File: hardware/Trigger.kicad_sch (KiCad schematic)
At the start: 4 parts, among them U6 MCP47FEB02A0T-E/ST, U7 Opamp_Dual

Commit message: added footprints
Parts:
- C28, C30: footprint (none) -> Capacitor_SMD:C_0402_1005Metric
- U6: footprint TSSOP8_ST_MCH -> MCP47FE:TSSOP8_ST_MCH
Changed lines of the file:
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@@
 			)
 		)
-		(property "Footprint" ""
+		(property "Footprint" "Capacitor_SMD:C_0402_1005Metric"
 			(at 43.4848 96.52 0)
 			(effects
@@
 			)
 		)
-		(property "Footprint" "TSSOP8_ST_MCH"
+		(property "Footprint" "MCP47FE:TSSOP8_ST_MCH"
 			(at 60.96 83.82 0)
 			(effects
@@
 			)
 		)
-		(property "Footprint" ""
+		(property "Footprint" "Capacitor_SMD:C_0402_1005Metric"
 			(at 141.9352 72.39 0)
 			(effects

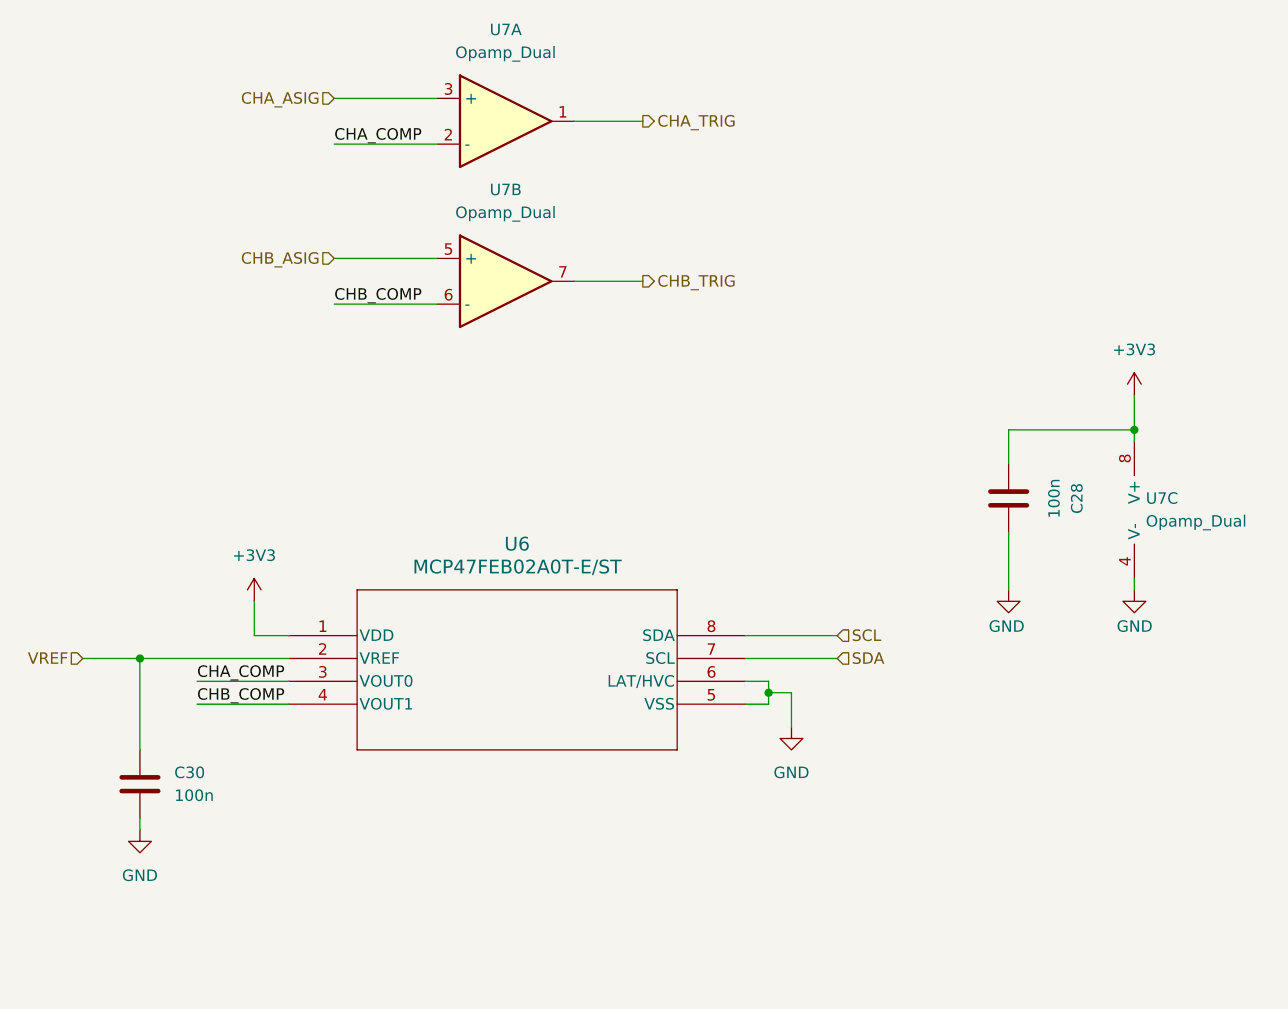
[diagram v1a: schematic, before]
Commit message: feat(hardware): Add test point connections + update PCB layout
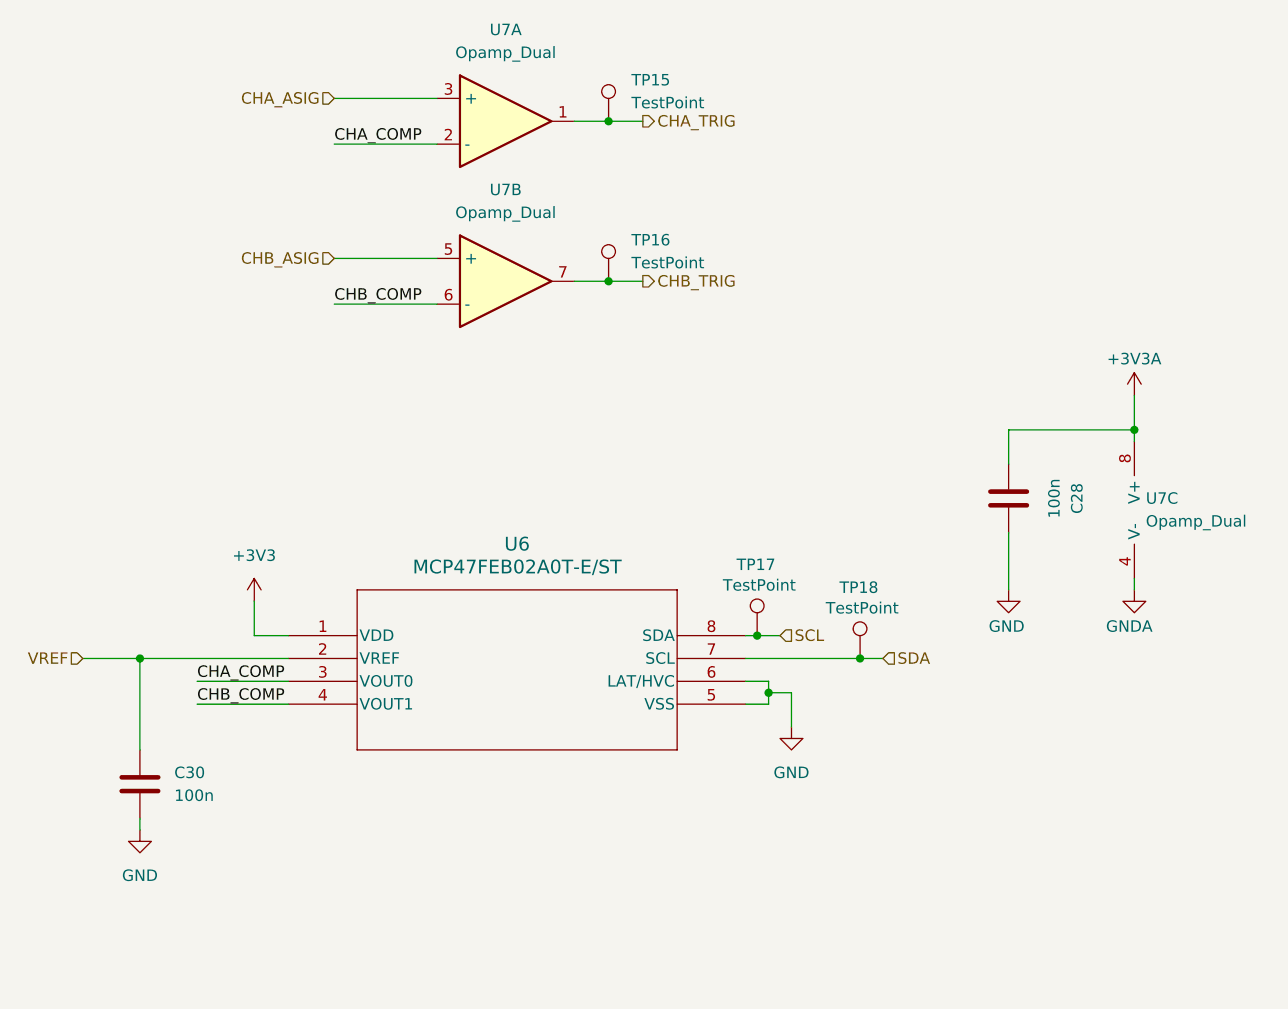
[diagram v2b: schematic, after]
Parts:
- added TP15, TP16, TP17, TP18: TestPoint, CustomTestPoints:TestPoint_0603_1608Metric, symbol Connector:TestPoint
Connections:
- net +3V3: no longer C28.1, U7.8 (V+)
- net CHA_TRIG: now also TP15.1
- net CHB_TRIG: now also TP16.1
- net GND: no longer U7.4 (V-)
- net SCL: now also TP17.1
- net SDA: now also TP18.1
- new net +3V3A: C28.1, U7.8 (V+)
- new net GNDA: U7.4 (V-)

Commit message: feat(hardware): Update PCB layout for power and trigger blocks
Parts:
- U7: footprint Package_DIP:DIP-8_W7.62mm_Socket_LongPads -> MCP6572T_E_SN:SOIC127P600X175-8N
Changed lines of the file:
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@@
 			)
 		)
-		(property "Footprint" "Package_DIP:DIP-8_W7.62mm_Socket_LongPads"
+		(property "Footprint" "MCP6572T_E_SN:SOIC127P600X175-8N"
 			(at 157.48 69.85 0)
 			(effects
@@
 			)
 		)
-		(property "Footprint" "Package_DIP:DIP-8_W7.62mm_Socket_LongPads"
+		(property "Footprint" "MCP6572T_E_SN:SOIC127P600X175-8N"
 			(at 85.09 26.67 0)
 			(effects
@@
 			)
 		)
-		(property "Footprint" "Package_DIP:DIP-8_W7.62mm_Socket_LongPads"
+		(property "Footprint" "MCP6572T_E_SN:SOIC127P600X175-8N"
 			(at 85.09 44.45 0)
 			(effects

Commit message: feat(hardware): Update switch footprint
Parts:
- TP15, TP16, TP17, TP18: Purchase Link (none) -> https://www.digikey.com/en/products/detail/koa-speer-electr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
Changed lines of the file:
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@@
+			)
+		)
+		(property "Purchase Link" "https://www.digikey.com/en/products/detail/koa-speer-electronics-inc/RCUCTE/11476561"
+			(at 96.52 44.45 0)
+			(effects
+				(font
+					(size 1.27 1.27)
+				)
+				(hide yes)
 			)
 		)
@@
 			)
 		)
+		(property "Purchase Link" "https://www.digikey.com/en/products/detail/koa-speer-electronics-inc/RCUCTE/11476561"
+			(at 96.52 26.67 0)
+			(effects
+				(font
+					(size 1.27 1.27)
+				)
+				(hide yes)
+			)
+		)
 		(pin "1"
 		)
@@
 			)
 		)
+		(property "Purchase Link" "https://www.digikey.com/en/products/detail/koa-speer-electronics-inc/RCUCTE/11476561"
+			(at 113.03 83.82 0)
+			(effects
+				(font
+					(size 1.27 1.27)
+				)
+				(hide yes)
+			)
+		)
 		(pin "1"
 		)
@@
 			(at 124.46 86.36 0)
 			(effects
+				(font
+					(size 1.27 1.27)
+				)
+				(hide yes)
+			)
+		)
+		(property "Purchase Link" "https://www.digikey.com/en/products/detail/koa-speer-electronics-inc/RCUCTE/11476561"
+			(at 124.46 86.36 0)
+			(effects

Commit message: feat(hardware): Finish component layout
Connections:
- net GND: no longer C28.2
- net GNDA: now also C28.2
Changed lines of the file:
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@@
 			)
 		)
-		(property "Value" "GND"
+		(property "Value" "GNDA"
 			(at 142.748 82.804 0)
 			(effects

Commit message: feat(hardware): updted design rules
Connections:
- net GNDA is gone; now on net GND: C28.2, U7.4 (V-)
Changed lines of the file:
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@@
 			)
 		)
-		(property "Value" "GNDA"
-			(at 156.972 82.804 0)
-			(effects
-				(font
-					(size 1.27 1.27)
-				)
-				(justify right)
+		(property "Value" "GND"
+			(at 154.94 82.55 0)
+			(effects
+				(font
+					(size 1.27 1.27)
+				)
 			)
 		)
@@
 			)
 		)
-		(property "Value" "GNDA"
-			(at 142.748 82.804 0)
-			(effects
-				(font
-					(size 1.27 1.27)
-				)
-				(justify right)
-			)
-		)
+		(property "Value" "GND"
+			(at 140.97 82.55 0)
+			(effects
+				(font
+					(size 1.27 1.27)
+				)
+			)
+		)

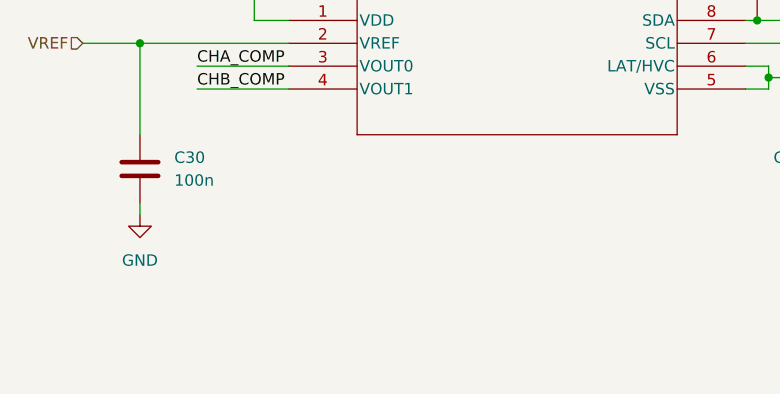
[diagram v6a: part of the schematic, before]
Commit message: feat(hardware): Add 1v65 rail on 4th plane
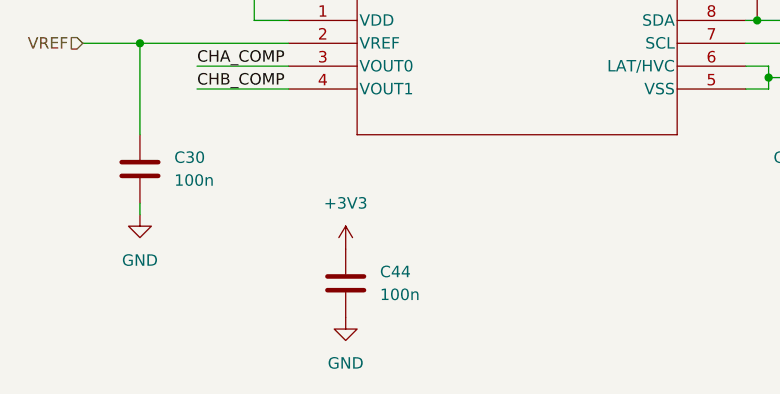
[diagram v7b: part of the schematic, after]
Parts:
- added C44: 100n, Capacitor_SMD:C_0402_1005Metric, symbol Device:C
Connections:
- net +3V3: now also C44.2
- net GND: now also C44.1
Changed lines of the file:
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@@
+	)
+	(symbol
+		(lib_id "Device:C")
+		(at 67.31 113.03 180)
+		(unit 1)
+		(exclude_from_sim no)
+		(in_bom yes)
+		(on_board yes)
+		(dnp no)
+		(fields_autoplaced yes)
+		(property "Reference" "C44"
+			(at 71.12 111.7599 0)
+			(effects
+				(font
+					(size 1.27 1.27)
+				)
+				(justify right)
+			)
+		)
+		(property "Value" "100n"
+			(at 71.12 114.2999 0)
+			(effects
+				(font
+					(size 1.27 1.27)
+				)
+				(justify right)
+			)
+		)
+		(property "Footprint" "Capacitor_SMD:C_0402_1005Metric"
+			(at 66.3448 109.22 0)
+			(effects
+				(font
+					(size 1.27 1.27)
+				)
+				(hide yes)
+			)
+		)
+		(property "Datasheet" "~"
+			(at 67.31 113.03 0)
+			(effects
+				(font
+					(size 1.27 1.27)
+				)
+				(hide yes)
+			)
+		)
+		(property "Description" "Unpolarized capacitor"
+			(at 67.31 113.03 0)
+			(effects
+				(font
+					(size 1.27 1.27)
+				)
+				(hide yes)
+			)
+		)
+		(pin "1"
+		)
+		(pin "2"
+		)
+		(instances
+			(project "RP2350_60QFN_minimal"
+				(path "/94683f5c-9cd9-448e-be96-9792537b5cb8/865345ee-93ca-410b-9293-676d9f6f2ef0"
+					(reference "C44")
+					(unit 1)
+				)
+			)
+		)
 	)
 	(symbol
@@
 	)
 	(symbol
+		(lib_id "power:+3V3")
+		(at 67.31 109.22 0)
+		(unit 1)
+		(exclude_from_sim no)
+		(in_bom yes)
+		(on_board yes)
+		(dnp no)
+		(fields_autoplaced yes)
+		(property "Reference" "#PWR0120"
+			(at 67.31 113.03 0)
+			(effects
+				(font
+					(size 1.27 1.27)
+				)
+				(hide yes)
+			)
+		)
+		(property "Value" "+3V3"
+			(at 67.31 104.14 0)
+			(effects
+				(font
+					(size 1.27 1.27)
+				)
+			)
+		)
+		(property "Footprint" ""
+			(at 67.31 109.22 0)
+			(effects
+				(font
+					(size 1.27 1.27)
+				)
+				(hide yes)
+			)
+		)
+		(property "Datasheet" ""
+			(at 67.31 109.22 0)
+			(effects
+				(font
+					(size 1.27 1.27)
+				)
+				(hide yes)
+			)
+		)
+		(property "Description" "Power symbol creates a global label with name \"+3V3\""
+			(at 67.31 109.22 0)
+			(effects
+				(font
+					(size 1.27 1.27)
+				)
+				(hide yes)
+			)
+		)
+		(pin "1"
+		)
+		(instances
+			(project "RP2350_60QFN_minimal"
+				(path "/94683f5c-9cd9-448e-be96-9792537b5cb8/865345ee-93ca-410b-9293-676d9f6f2ef0"
+					(reference "#PWR0120")
+					(unit 1)
+				)
+			)
+		)
+	)
+	(symbol
 		(lib_id "Device:C")
 		(at 44.45 100.33 180)
@@
 					(unit 1)
 				)
+			)
+		)
+	)
+	(symbol
+		(lib_id "power:GND")
+		(at 67.31 116.84 0)
+		(unit 1)
+		(exclude_from_sim no)
+		(in_bom yes)
+		(on_board yes)
+		(dnp no)
+		(fields_autoplaced yes)
+		(property "Reference" "#PWR0121"
+			(at 67.31 123.19 0)
+			(effects
+				(font
+					(size 1.27 1.27)
+				)
+				(hide yes)
+			)
+		)
+		(property "Value" "GND"
+			(at 67.31 121.92 0)
+			(effects
+				(font
+					(size 1.27 1.27)
+				)
+			)
+		)
+		(property "Footprint" ""
+			(at 67.31 116.84 0)
+			(effects
+				(font
+					(size 1.27 1.27)
+				)
+				(hide yes)
+			)
+		)
+		(property "Datasheet" ""
+			(at 67.31 116.84 0)
+			(effects
+				(font
+					(size 1.27 1.27)
+				)
+				(hide yes)
+			)
+		)
+		(property "Description" "Power symbol creates a global label with name \"GND\" , ground"
+			(at 67.31 116.84 0)
+			(effects
+				(font
+					(size 1.27 1.27)
+				)
+				(hide yes)
+			)
+		)
+		(pin "1"
+		)
+		(instances
+			(project "RP2350_60QFN_minimal"
+				(path "/94683f5c-9cd9-448e-be96-9792537b5cb8/865345ee-93ca-410b-9293-676d9f6f2ef0"
+					(reference "#PWR0121")
+					(unit 1)
+				)

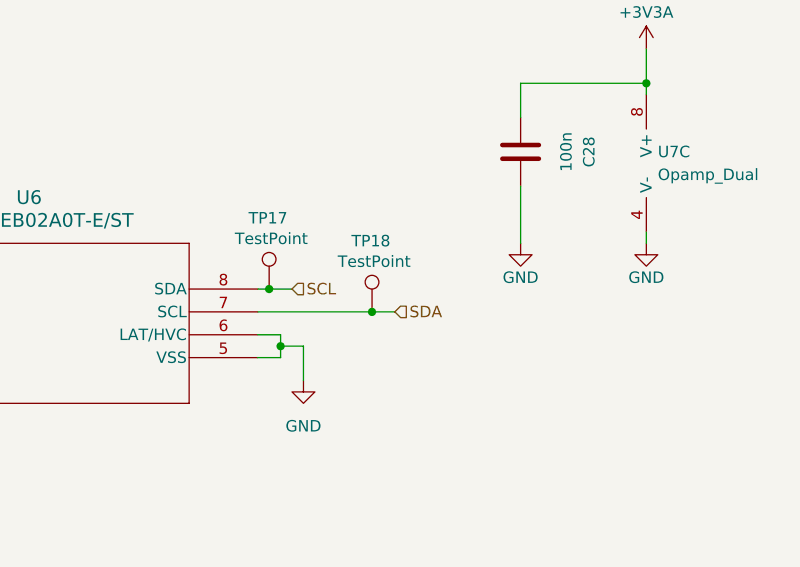
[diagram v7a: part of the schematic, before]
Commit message: changed pcb size, added pull up resistors to I2C, fixed OPA320 footprints/schematic
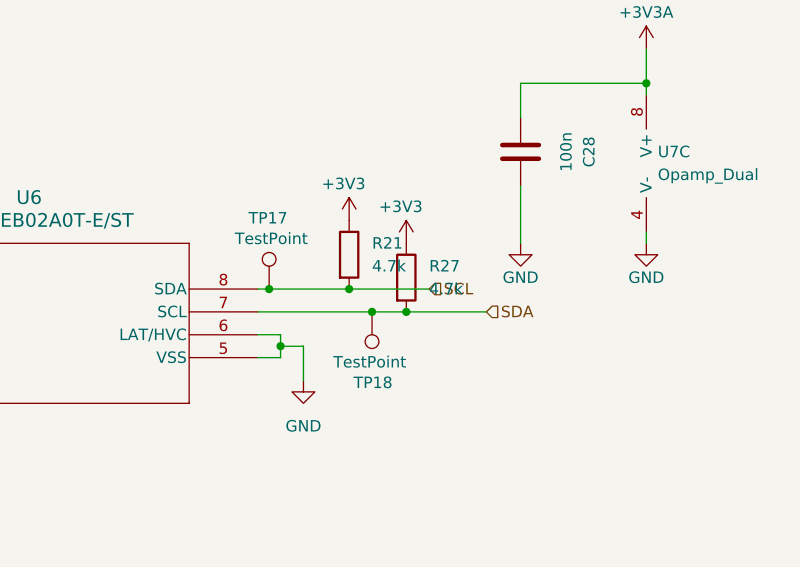
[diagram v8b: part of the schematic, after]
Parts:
- added R21, R27: 4.7k, Resistor_SMD:R_0402_1005Metric, symbol Device:R
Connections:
- net +3V3: now also R21.1, R27.1
- net SCL: now also R21.2
- net SDA: now also R27.2
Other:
- moved on the sheet: TP18
